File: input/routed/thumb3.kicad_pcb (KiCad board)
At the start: 2 copper layers, 20 x 51 mm, 12 parts, among them T1 Flactyl 5.0 (thumb3), T2 x, T3 y

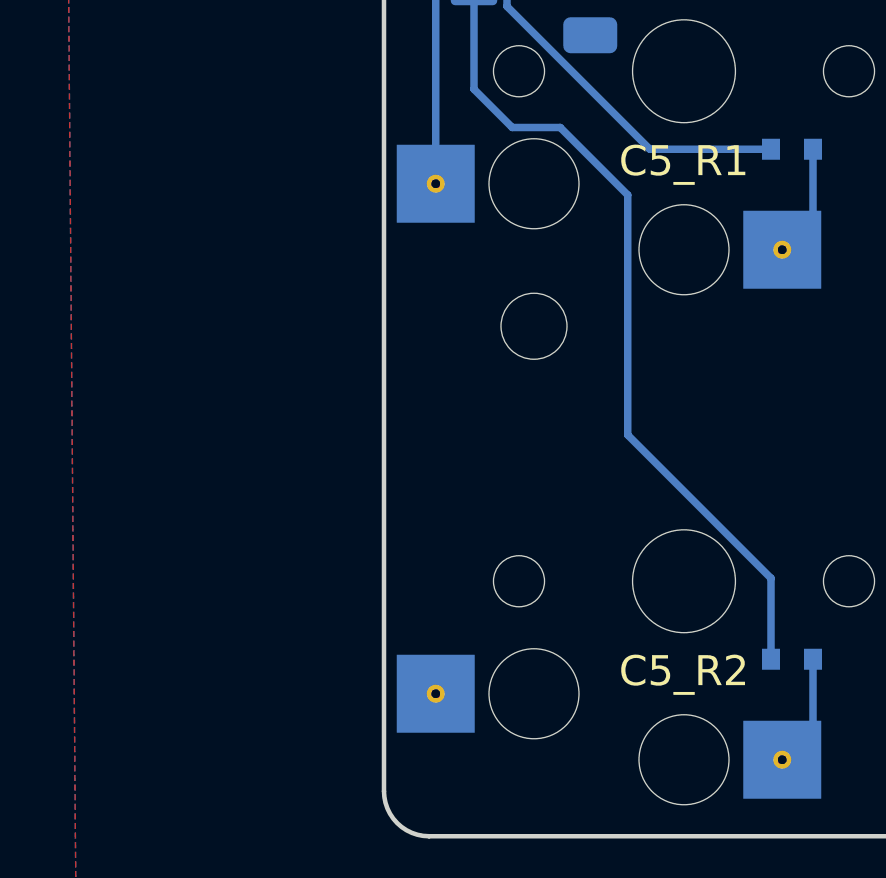
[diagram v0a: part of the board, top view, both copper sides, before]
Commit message: move thumb cutout
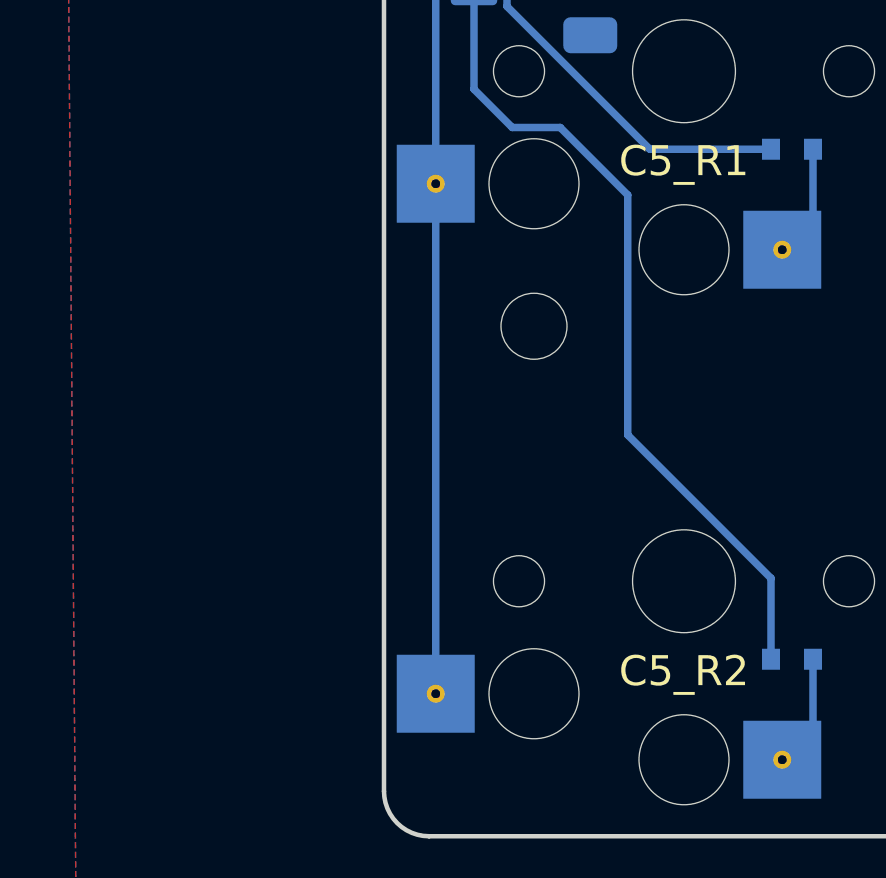
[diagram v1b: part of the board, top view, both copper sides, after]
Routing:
- net C5: track 45.0 -> 62.0 mm
